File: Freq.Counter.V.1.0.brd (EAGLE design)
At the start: 99 x 94.9 mm, 15 parts, among them IC1 MEGA8-P, IC2 7805TV, IC3 74HC93N, Q1 16M

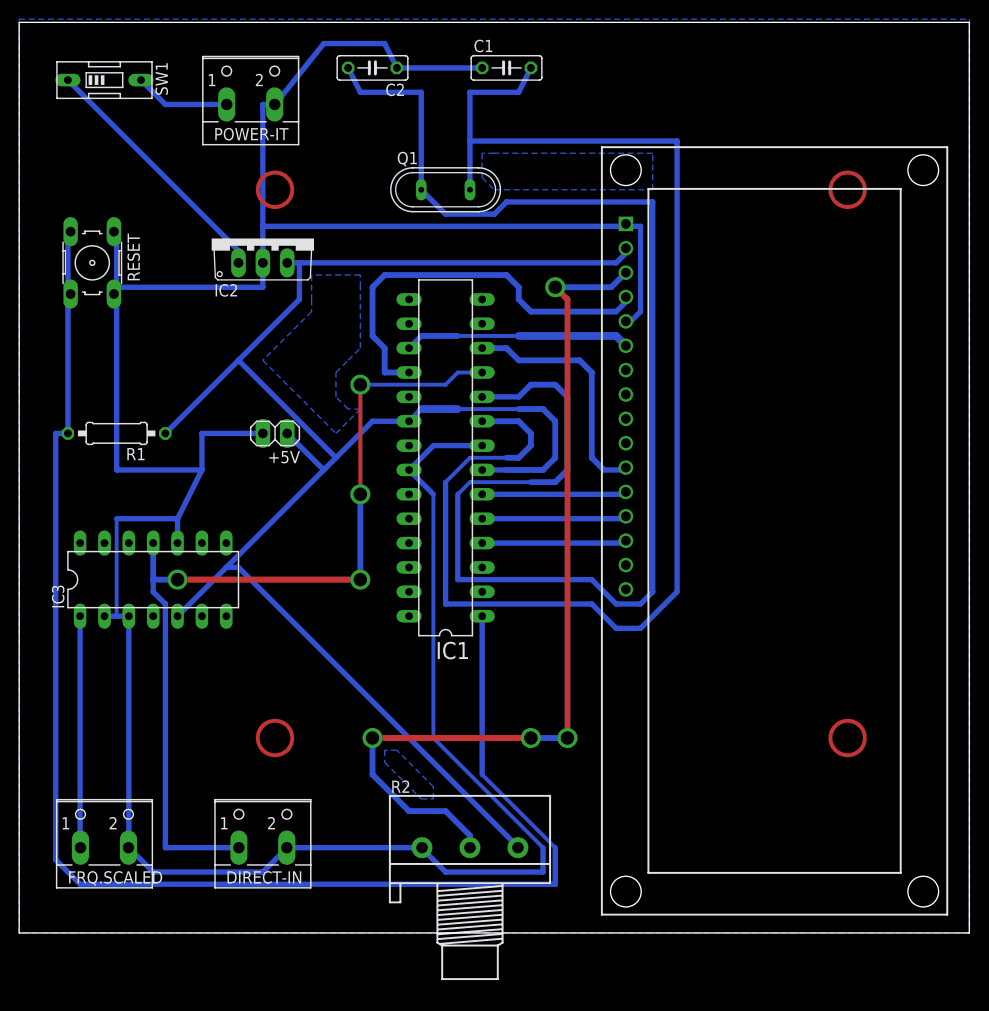
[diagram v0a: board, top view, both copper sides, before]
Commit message: Arduino Freq. Counter (up to 64 Mhz) V.1.1
Arduino Freq. Counter (up to 64 Mhz) V.1.1
With smaller PCB
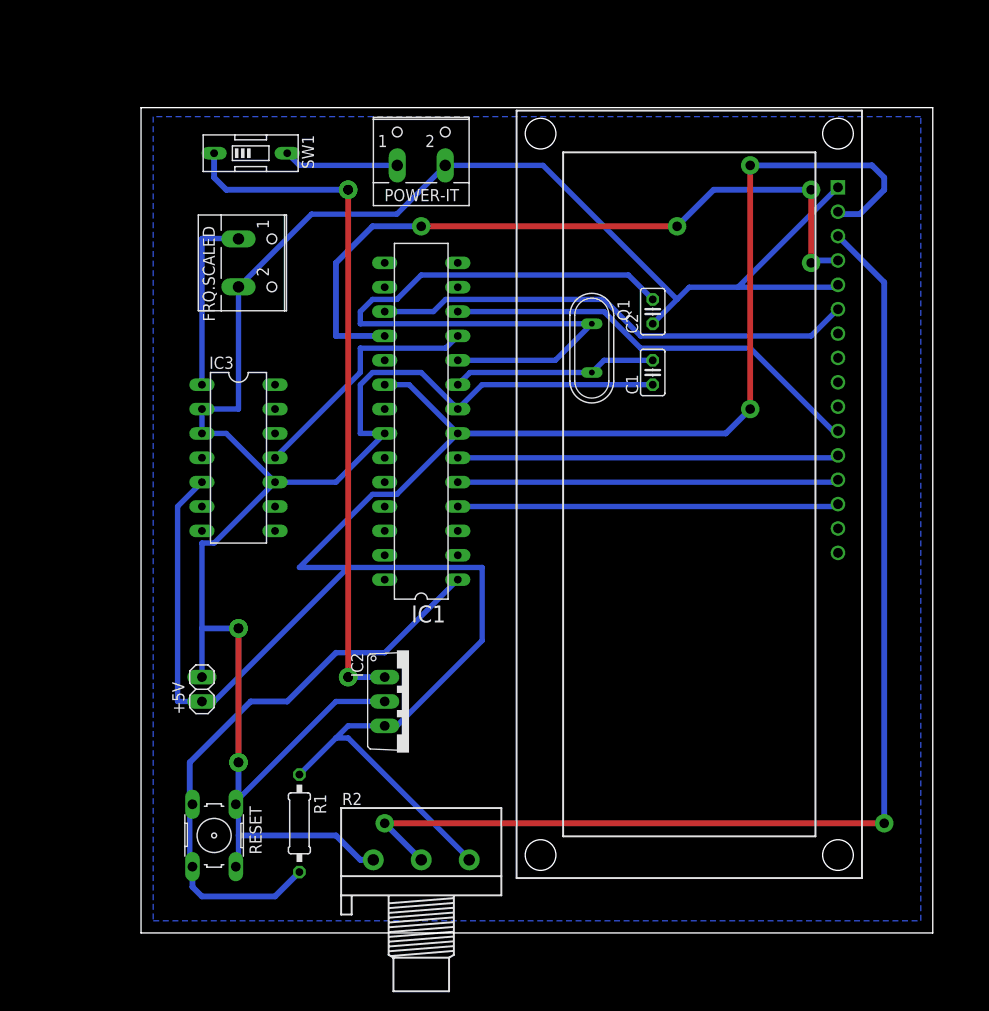
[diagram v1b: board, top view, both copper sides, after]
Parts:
- removed DIRECT-IN: (no value), con-wago-500:W237-102
- C1, C2: device rcl:C050-025X075 -> rcl:C025-025X050
- U$1: value LCD-HD4478016X2-4-HOLES-BL16X2-4-HOLES-BL -> LCD-HD447804-HOLES16X2-4-HOLES; device HD44780LCD:LCD-16X2-4HOLES-BL -> LCD-Library-EagleCAD-HD44780:LCD-16X2-4HOLES
- moved FRQ.SCALED 61.6 mm to (24.1, 58.4), turned to 270 degrees
- moved RESET 61.0 mm to (20.3, -1.27)
- moved IC2 50.6 mm to (40.6, 12.7), turned to 270 degrees
- moved R1 44.9 mm to (29.2, 0.00), turned to 270 degrees
- moved C2 38.7 mm to (66.0, 53.3), turned to 90 degrees
- moved C1 35.2 mm to (66.0, 47.0), turned to 90 degrees
- moved +5V 27.7 mm to (19.1, 14.0), turned to 90 degrees
- moved Q1 22.5 mm to (59.7, 49.5), turned to 270 degrees
- moved POWER-IT 18.9 mm to (41.9, 69.8)
- moved SW1 17.0 mm to (24.1, 69.8)
- moved IC3 15.5 mm to (22.9, 38.1), turned to 270 degrees
- moved U$1 9.67 mm to (69.8, 34.3)
- moved R2 5.24 mm to (41.9, -3.81)
- moved IC1 4.58 mm to (41.9, 41.9)
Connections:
- net ARDUINO-IN: no longer DIRECT-IN.1
- net GND: no longer DIRECT-IN.2
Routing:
- net N$5: track 143.5 -> 21.4 mm
- net N$1: track 151.1 -> 61.6 mm
- net N$6: track 146.5 -> 74.1 mm
- net ARDUINO-IN: track 95.1 -> 25.8 mm, vias 4 -> 0
- net GND: track 310.9 -> 263.7 mm, vias 0 -> 2
- net +5V: track 183.2 -> 229.0 mm, vias 0 -> 2
- net N$2: track 26.4 -> 71.6 mm, vias 0 -> 2
- net D12: track 42.4 -> 75.9 mm, vias 0 -> 4
- net POT: track 93.7 -> 120.7 mm, vias 12 -> 2
- net D11: track 23.6 -> 50.5 mm
- net D4: track 15.6 -> 39.7 mm
- net D3: track 15.6 -> 39.7 mm
- net D2: track 15.6 -> 39.7 mm
- net D6: track 26.1 -> 45.0 mm
- net N$3: track 24.2 -> 19.1 mm
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- removed copper zone on layer 16, net N$4
- removed copper zone on layer 16, net N$7
- removed copper zone on layer 16, net N$8
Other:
- board size 99 x 94.9 mm -> 82.5 x 86 mm
